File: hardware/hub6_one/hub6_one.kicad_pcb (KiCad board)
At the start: 2 copper layers, 61.1 x 58.1 mm, 10 parts, among them J1 plate 1, J2 plate 2, J3 plate 3, J4 plate 4, J5 plate 5, J6 base, U1 74HC138, U2 XIAO ESP32S3

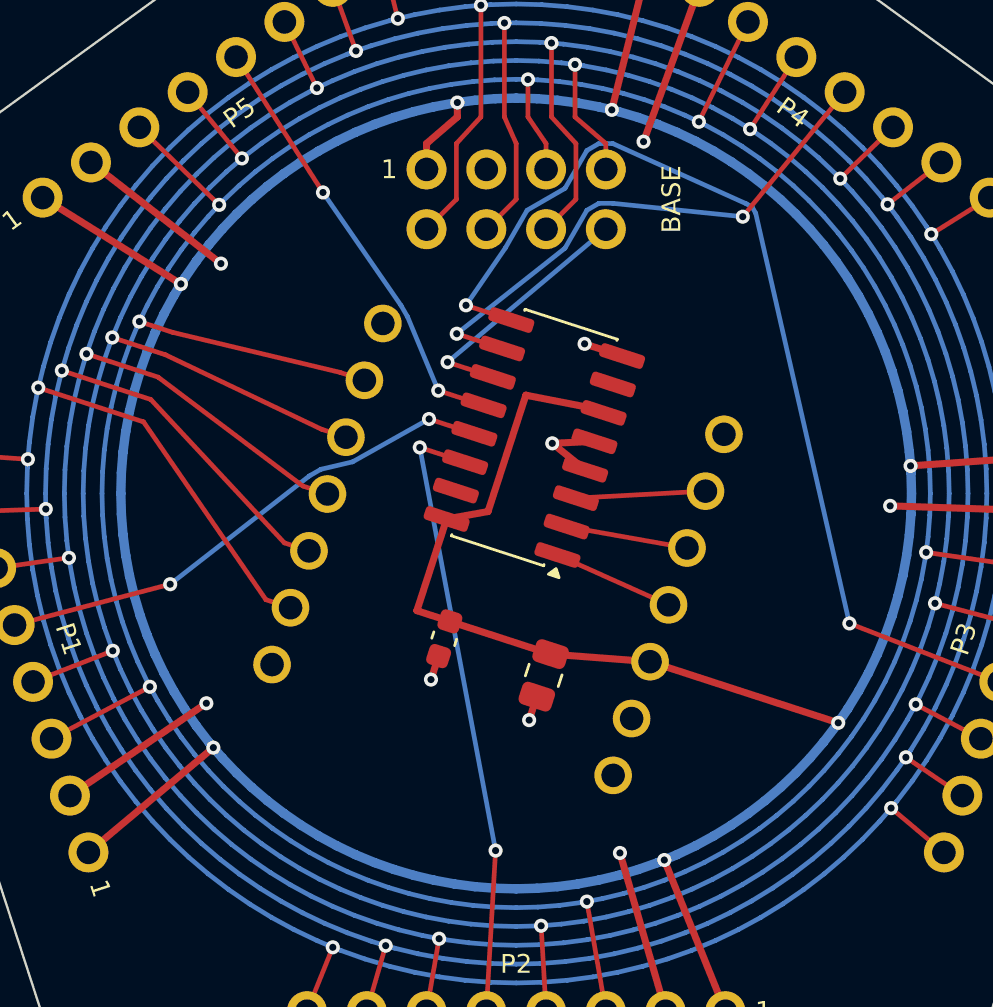
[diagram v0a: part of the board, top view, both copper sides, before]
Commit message: hub6_one: the XIAO in two female sockets under the board, parts as hub3's
The XIAO now plugs into two 1x7 8.5 mm female sockets (C2832270) on the underside,
3 mm off the middle toward 342 degrees so that, hanging lower, it clears the base
display's plug: with the connectors as they are (top entry, 3 mm proud of the plate,
the plug 2 mm more; tmp/connectors.py) nothing touches, 1.5 mm to the nearest. Plate 3's
chip select goes round the chip's USB-C end now (Y0); P1 Y2, P2 Y1, P3 Y0, P4 Y5, P5 Y3,
base Y4. U1 is C2674688, as on cubic-earth's hub3 (the capacitors and sockets were
already the same). fab.py writes the sockets as bottom-side parts. ERC, DRC, parity clean.

Claude-Session: https://claude.ai/code/session_01WVeYczw2dnncq6csD58pZW
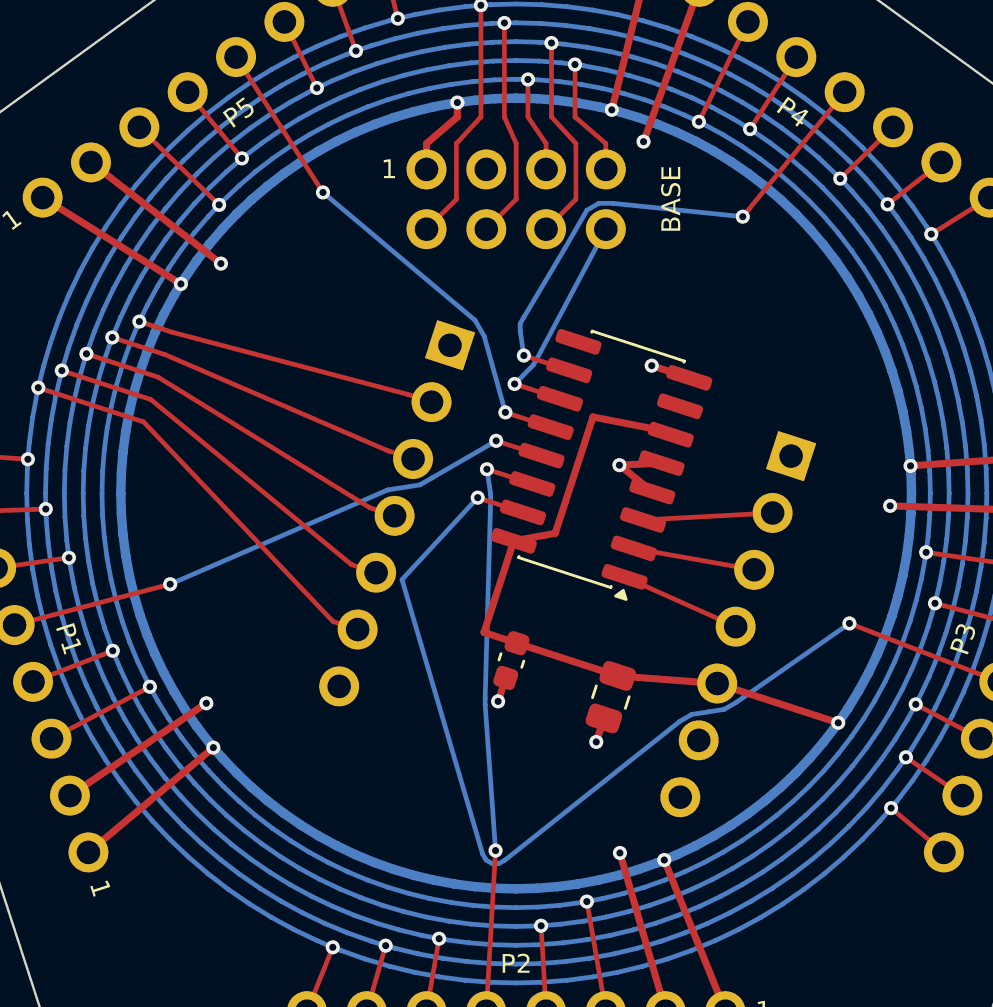
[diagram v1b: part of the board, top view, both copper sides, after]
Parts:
- removed U2: XIAO ESP32S3, dodecahedron-earth:XIAO_ESP32S3_Hanging
- added J7: XIAO D0-D6, Connector_PinSocket_2.54mm:PinSocket_1x07_P2.54mm_Vertical, B.Cu at (129.3, 125.8)
- added J8: XIAO 5V-D7, Connector_PinSocket_2.54mm:PinSocket_1x07_P2.54mm_Vertical, B.Cu at (143.8, 130.6)
- added X1: XIAO, dodecahedron-earth:XIAO_ESP32S3_Hanging, F.Cu at (134.2, 135.4)
- moved U1 3.00 mm to (135.8, 130.7)
- moved C2 3.00 mm to (136.2, 140.8)
- moved C3 3.00 mm to (131.9, 139.2)
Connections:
- U1 pad 15: unconnected-(U1-Y0-Pad15) -> LCD_CS2
- U1 pad 9: LCD_CS2 -> unconnected-(U1-Y6-Pad9)
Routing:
- net +3V3: track 176.7 -> 173.7 mm
- net LCD_DIN: track 148.2 -> 151.2 mm
- net LCD_CLK: track 149.7 -> 152.6 mm
- net LCD_DC: track 157.1 -> 160.0 mm
- net LCD_CS4: track 18.7 -> 21.4 mm
- net LCD_RST: track 162.9 -> 165.7 mm
- net LCD_BL: track 170.7 -> 173.3 mm
- net LCD_CS0: track 22.0 -> 24.1 mm
- net LCD_CS2: track 43.3 -> 44.9 mm
- net LCD_CS1: track 26.3 -> 25.1 mm
- net LCD_CS5: track 10.8 -> 9.70 mm
- net LCD_CS3: track 23.3 -> 22.6 mm

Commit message: hub6_one: each cable hole's signal on the silkscreen, both sides
VCC, GND, DIN, CLK, CS, DC, RST, BL beside every hole of the six cable rows: just outside
each side row's holes, reading outward, and outward of J6's outer row and inward of its
inner row; on the top and the bottom, since the side cables come from above and the base
cable from below. A wire in the wrong hole is the easy mistake. DRC clean; fab6 rebuilt.

Claude-Session: https://claude.ai/code/session_01WVeYczw2dnncq6csD58pZW
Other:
- board text added: "BL"
- board text added: "CLK"
- board text added: "CS"
- board text added: "DC"
- board text added: "DIN"
- board text added: "GND"
- board text added: "RST"
- board text added: "VCC"

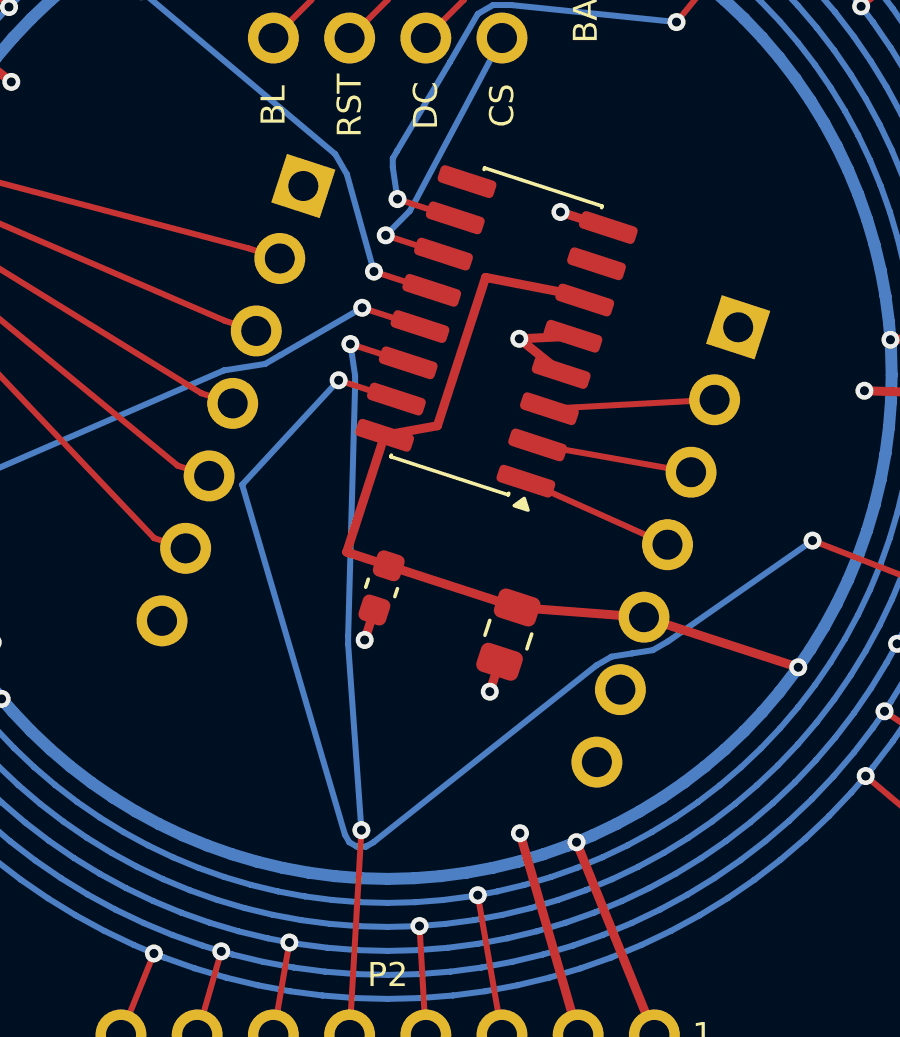
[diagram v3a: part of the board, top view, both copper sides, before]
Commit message: hub6_one: the XIAO's pin names and its USB-C end on the silkscreen
Two 1x7 sockets take the XIAO turned round as well, so both sides now show each socket
pin's name (D0..D6; 5V, GND, 3V3, D10..D7) between the sockets, and an outline of the
USB-C with "XIAO USB-C" beyond the end it goes. Seen from below, as it is plugged in, the
names read as Seeed's front pinout turned round. C2 moves 1.2 mm inward, clear of a name.
DRC clean; fab6 rebuilt.

Claude-Session: https://claude.ai/code/session_01WVeYczw2dnncq6csD58pZW
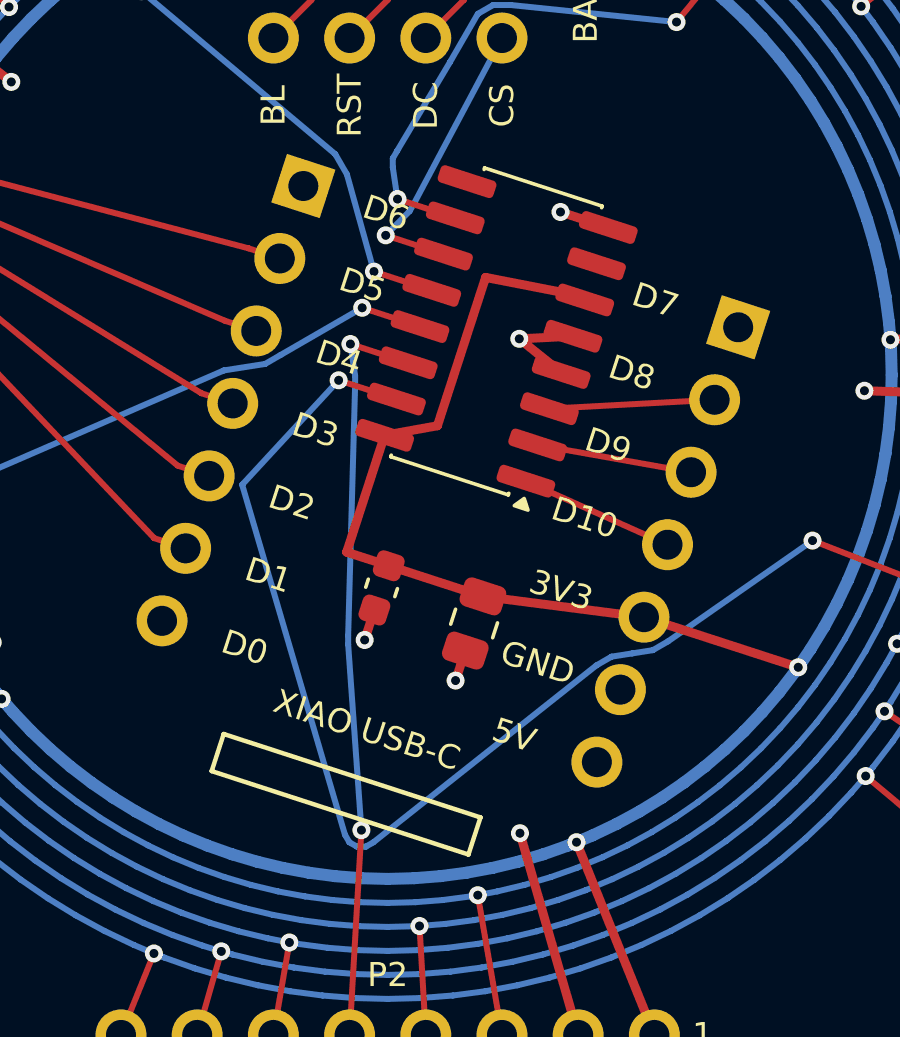
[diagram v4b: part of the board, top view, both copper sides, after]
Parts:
- moved C2 1.20 mm to (135.0, 140.4)
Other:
- board text added: "3V3"
- board text added: "5V"
- board text added: "D0"
- board text added: "D1"
- board text added: "D10"
- board text added: "D2"
- board text added: "D3"
- board text added: "D4"
- board text added: "D5"
- board text added: "D6"
- board text added: "D7"
- board text added: "D8"
- board text added: "D9"
- board text added: "XIAO USB-C"
